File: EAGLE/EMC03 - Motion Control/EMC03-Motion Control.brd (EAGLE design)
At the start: 100 x 86.6 mm, 132 parts, among them J1 UART0, J10 S4B-PH-SM4, J11 S4B-PH-SM4, J12 S4B-PH-SM4, J13 S5B-PH-SM4, J14 S5B-PH-SM4, J15 S5B-PH-SM4, J17 S8B-PH-SM4, J19 S6B-PH-SM4, J2 FTSH-105-1-L-DV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

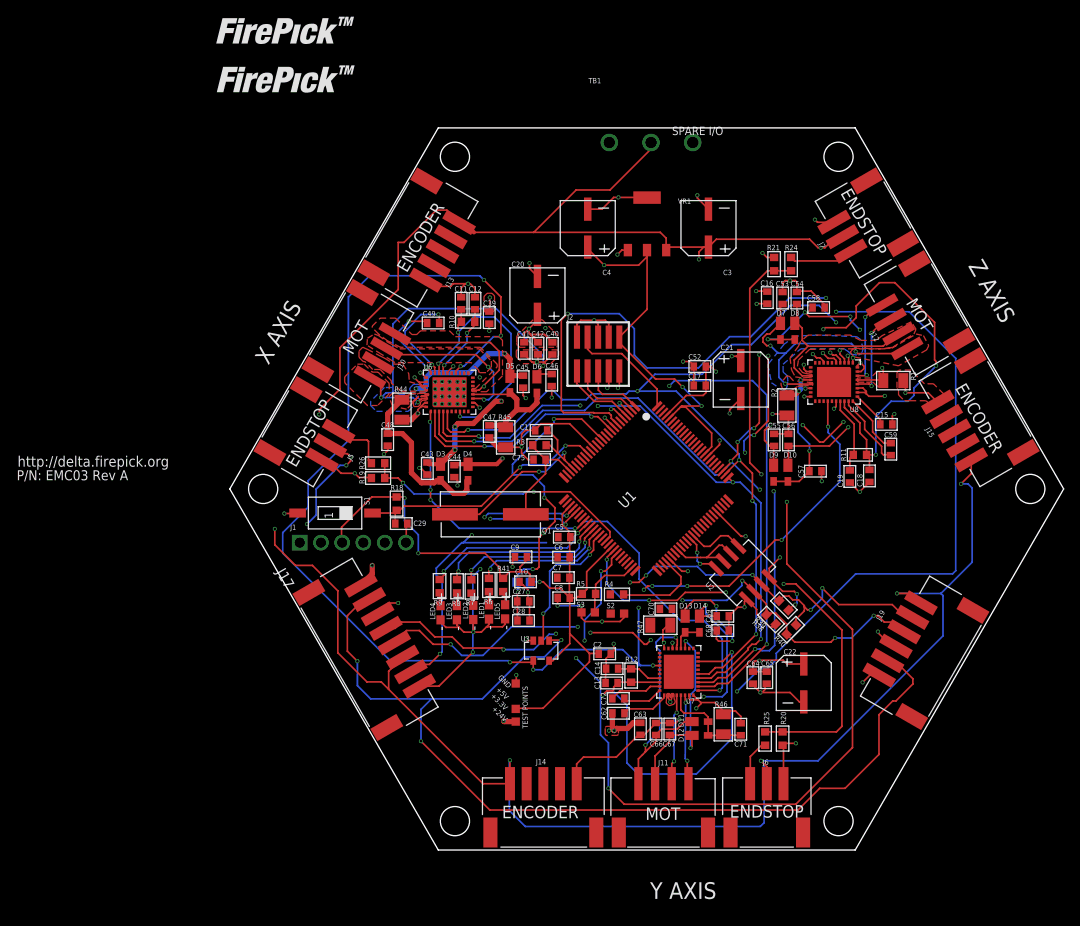
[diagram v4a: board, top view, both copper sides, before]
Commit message: Completed boards. Please look at airwires connecting thermal pads to GND vias. They shouldn't be present due to the vias.
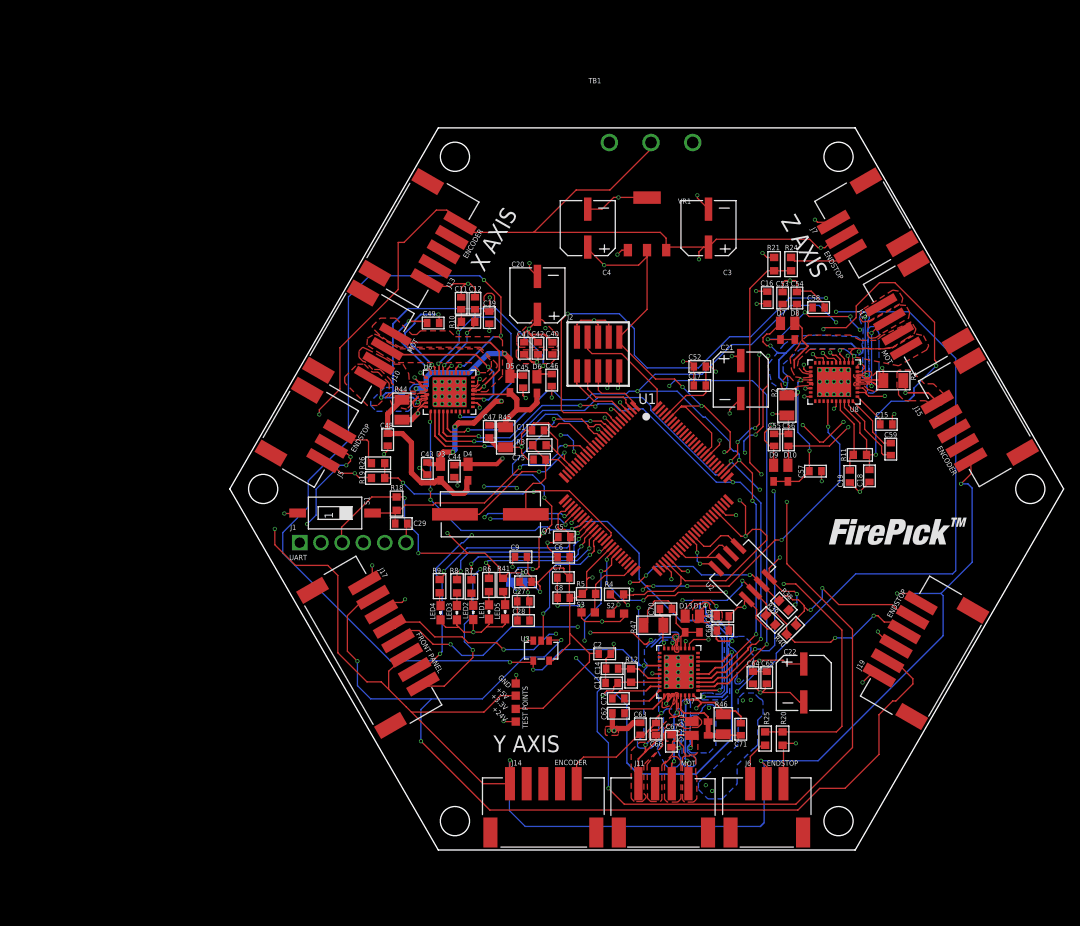
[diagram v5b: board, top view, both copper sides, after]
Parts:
- removed LOGO10: LOGO-FIREPICKLARGE, FirePick:LOGO-FIREPICK
- added TP2: +3.3V, TinWhiskers:TESTPAD
- moved LOGO12 94.9 mm to (71.6, 41.6)
- moved LOGO1 27.4 mm to (86.4, 41.4)
- moved C67 1.47 mm to (53.0, 19.7), turned to 270 degrees
- moved R47 0.83 mm to (50.8, 33.7)
- moved FB2 0.76 mm to (34.4, 38.8)
- moved J17 0.51 mm to (19.7, 32.7)
- moved C1 0.38 mm to (37.0, 57.0)
- moved J13 0.14 mm to (25.6, 78.4)
- moved J5 0.14 mm to (12.2, 55.1)
- moved J12 0.12 mm to (79.6, 69.5)
- moved J10 0.09 mm to (18.4, 65.9)
- moved R39 0.09 mm to (64.8, 34.3)
- moved J15 0.08 mm to (86.8, 57.0)
- moved J7 0.06 mm to (73.4, 80.2)
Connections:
- net +5V: now also TP2.PAD
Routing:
- net +3V3: track 166.0 -> 244.0 mm, vias 10 -> 20
- net 2A_2: track 25.3 -> 5.25 mm, vias 2 -> 3
- net 2B_2: track 29.8 -> 14.3 mm
- net GND: track 236.2 -> 251.5 mm, vias 58 -> 111
- net +5V: track 291.7 -> 306.6 mm
- net ISP_COM: track 0.00 -> 14.0 mm, vias 0 -> 3
- net 2A_3: track 23.4 -> 9.73 mm
- net USBMCU+: track 45.0 -> 34.6 mm
- net BRB2: track 3.87 -> 13.7 mm
- net 2B_3: track 32.5 -> 23.3 mm
- net DPWR: track 39.5 -> 44.3 mm
- net +24V: track 51.6 -> 53.1 mm, vias 17 -> 18
- net CLK: track 149.5 -> 150.4 mm
- net STAT_LED4: track 16.5 -> 17.4 mm
- net USBMCU-: track 36.4 -> 37.2 mm
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- added copper zone on layer 1, net 1A_2
- added copper zone on layer 15, net 1A_2
- added copper zone on layer 16, net 1A_2
- added copper zone on layer 1, net 1A_3
- added copper zone on layer 16, net 1A_3
- added copper zone on layer 1, net 1B_2
- added copper zone on layer 15, net 1B_2
- added copper zone on layer 16, net 1B_2
- added copper zone on layer 1, net 1B_3
- added copper zone on layer 16, net 1B_3
- added copper zone on layer 1, net 2A_2
- added copper zone on layer 15, net 2A_2
- added copper zone on layer 16, net 2A_2
- added copper zone on layer 1, net 2B_2
- added copper zone on layer 16, net 2B_2
- added copper zone on layer 1, net N$7
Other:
- board text added: "FRONT PANEL"
- board text added: "UART"
- board text removed: "P/N: EMC03 Rev A"
- board text removed: "SPARE I/O"
- board text removed: "http://delta.firepick.org"

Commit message: Updated all boards to include changes for production
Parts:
- S1: value SWS001 -> CPL-SW-MOM-147873-2; device smd-special:SMS-001 -> TinWhiskers:147873-2
- S2, S3: device TinWhiskers:0603 -> TinWhiskers:147873-2
- moved C14 3.95 mm to (42.2, 26.9)
- moved C13 3.93 mm to (42.2, 25.2)
- moved R12 3.72 mm to (44.5, 27.1)
- moved S2 3.28 mm to (46.8, 31.8), turned to 90 degrees
- moved S3 2.45 mm to (40.6, 34.5)
- moved C2 1.40 mm to (43.6, 30.2)
- moved S1 0.73 mm to (13.1, 47.7), turned to 0 degrees
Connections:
- net +3V3: now also VR1.P$1; no longer VR1.2
- net GND: no longer VR1.P$1
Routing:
- net +3V3: track 244.0 -> 258.8 mm, vias 20 -> 23
- net 1B_2: track 31.5 -> 21.8 mm, vias 4 -> 6
- net 1A_2: track 24.2 -> 18.3 mm, vias 9 -> 11
- net N$5: track 5.45 -> 9.32 mm
- net 2B_2: track 14.3 -> 11.2 mm, vias 2 -> 3
- net N$6: track 48.0 -> 51.0 mm
- net RESET: track 31.8 -> 33.6 mm
- net 2A_2: track 5.25 -> 3.65 mm, vias 3 -> 6
- net DFU: track 8.60 -> 9.75 mm
- net B: track 76.5 -> 77.5 mm, vias 7 -> 8
- net ISP_COM: track 14.0 -> 15.0 mm
- net !ENABLE_LPC: track 17.3 -> 18.0 mm
- net GND: track 251.5 -> 251.2 mm, vias 111 -> 110

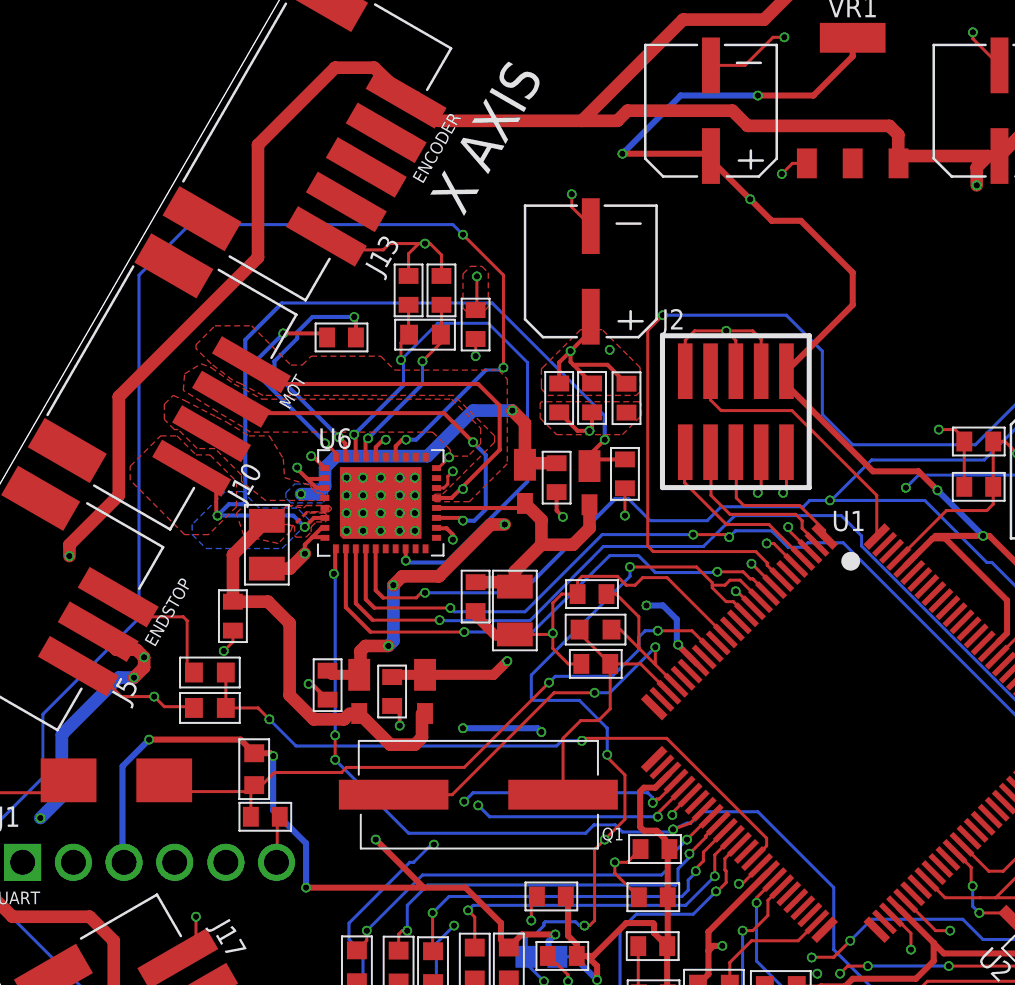
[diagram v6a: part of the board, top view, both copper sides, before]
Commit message: Updated motor hole size to 7mm Dia. Rerouted around.
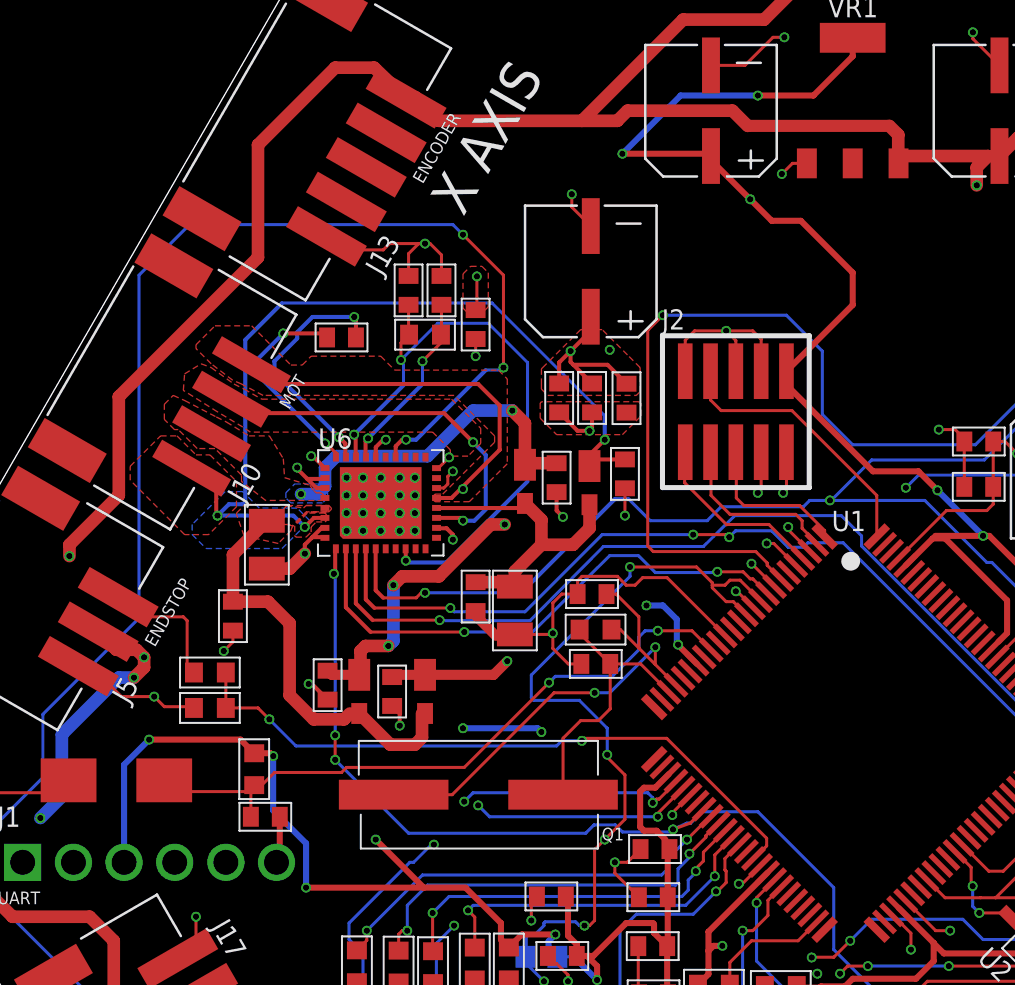
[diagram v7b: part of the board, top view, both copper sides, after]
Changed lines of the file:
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@@
 <layer number="23" name="tOrigins" color="15" fill="1" visible="yes" active="yes"/>
 <layer number="24" name="bOrigins" color="15" fill="1" visible="yes" active="yes"/>
-<layer number="25" name="tNames" color="7" fill="1" visible="yes" active="yes"/>
-<layer number="26" name="bNames" color="7" fill="1" visible="yes" active="yes"/>
+<layer number="25" name="tNames" color="7" fill="1" visible="no" active="yes"/>
+<layer number="26" name="bNames" color="7" fill="1" visible="no" active="yes"/>
 <layer number="27" name="tValues" color="7" fill="1" visible="no" active="yes"/>
 <layer number="28" name="bValues" color="7" fill="1" visible="no" active="yes"/>
-<layer number="29" name="tStop" color="7" fill="3" visible="yes" active="yes"/>
-<layer number="30" name="bStop" color="7" fill="6" visible="yes" active="yes"/>
-<layer number="31" name="tCream" color="7" fill="4" visible="yes" active="yes"/>
-<layer number="32" name="bCream" color="7" fill="5" visible="yes" active="yes"/>
+<layer number="29" name="tStop" color="7" fill="3" visible="no" active="yes"/>
+<layer number="30" name="bStop" color="7" fill="6" visible="no" active="yes"/>
+<layer number="31" name="tCream" color="7" fill="4" visible="no" active="yes"/>
+<layer number="32" name="bCream" color="7" fill="5" visible="no" active="yes"/>
 <layer number="33" name="tFinish" color="6" fill="3" visible="no" active="yes"/>
 <layer number="34" name="bFinish" color="6" fill="6" visible="no" active="yes"/>
@@
 <wire x1="41.529" y1="27.7495" x2="41.529" y2="26.887" width="0.2032" layer="1"/>
 <wire x1="41.529" y1="26.887" x2="41.5025" y2="26.8605" width="0.2032" layer="1"/>
-<wire x1="72.4535" y1="62.865" x2="72.463" y2="62.827" width="0" layer="19" extent="1-1"/>
-<wire x1="53.848" y1="28.067" x2="53.7845" y2="28.0035" width="0" layer="19" extent="1-1"/>
-<wire x1="26.3525" y1="61.595" x2="26.3525" y2="61.976" width="0" layer="19" extent="1-1"/>
 <wire x1="42.037" y1="28.2575" x2="43.053" y2="28.2575" width="0.2032" layer="1"/>
 <wire x1="43.053" y1="28.2575" x2="43.688" y2="28.8925" width="0.2032" layer="1"/>
@@
 <wire x1="6.5405" y1="47.0535" x2="10.065334375" y2="47.0535" width="0.1524" layer="1"/>
 <wire x1="10.065334375" y1="47.0535" x2="10.687128125" y2="47.67529375" width="0.1524" layer="1"/>
+<wire x1="72.4535" y1="62.865" x2="72.463" y2="62.827" width="0" layer="19" extent="1-1"/>
+<wire x1="53.848" y1="28.067" x2="53.7845" y2="28.0035" width="0" layer="19" extent="1-1"/>
+<wire x1="26.3525" y1="61.595" x2="26.3525" y2="61.976" width="0" layer="19" extent="1-1"/>
 </signal>
 <signal name="X_STOP">
@@
 <wire x1="28.0814" y1="81.9641" x2="29.2735" y2="80.772" width="0.635" layer="1"/>
 <wire x1="29.2735" y1="80.772" x2="36.449" y2="80.772" width="0.635" layer="1"/>
-<wire x1="51.6255" y1="80.772" x2="51.8795" y2="80.518" width="0" layer="19" extent="1-16"/>
 <wire x1="51.8795" y1="80.518" x2="52.324" y2="80.0735" width="0.635" layer="1"/>
 <wire x1="52.324" y1="80.0735" x2="52.324" y2="78.652" width="0.635" layer="1"/>
@@
 <wire x1="38.735" y1="81.28" x2="44.0055" y2="81.28" width="0.635" layer="1"/>
 <wire x1="44.0055" y1="81.28" x2="44.7675" y2="80.518" width="0.635" layer="1"/>
-<wire x1="44.7675" y1="80.518" x2="51.8795" y2="80.518" width="0.635" layer="1"/>
+<wire x1="44.7675" y1="80.518" x2="51.8795" y2="80.518" width="0.6096" layer="1"/>
 </signal>
 <signal name="Y_STOP">
@@
 <contactref element="J1" pad="6"/>
 <contactref element="C29" pad="1"/>
-<wire x1="21.1593" y1="43.5237" x2="21.1593" y2="45.72" width="0.1524" layer="1"/>
-<wire x1="21.1593" y1="45.72" x2="21.2863" y2="45.847" width="0.1524" layer="1"/>
-<wire x1="21.1593" y1="43.5237" x2="21.122" y2="43.561" width="0" layer="19" extent="1-1"/>
+<wire x1="21.2863" y1="45.847" x2="21.2863" y2="43.7253" width="0.3048" layer="1"/>
+<wire x1="21.2863" y1="43.7253" x2="21.122" y2="43.561" width="0.3048" layer="1"/>
 </signal>
 <signal name="+3V3">
@@
 <wire x1="39.751" y1="28.8925" x2="38.8025" y2="28.8925" width="0.3048" layer="1"/>
 <wire x1="38.8025" y1="28.8925" x2="38.288" y2="29.407" width="0.3048" layer="1"/>
-<wire x1="13.3985" y1="43.6345" x2="13.3985" y2="48.387" width="0.3048" layer="16"/>
-<wire x1="13.3985" y1="48.387" x2="14.732" y2="49.7205" width="0.3048" layer="16"/>
 <via x="14.732" y="49.7205" extent="1-16" drill="0.3048"/>
 <wire x1="14.732" y1="49.7205" x2="19.317503125" y2="49.7205" width="0.3048" layer="1"/>
 <wire x1="19.317503125" y1="49.7205" x2="20.0025" y2="49.035503125" width="0.3048" layer="1"/>
-<wire x1="13.3985" y1="43.6345" x2="13.472" y2="43.561" width="0" layer="19" extent="16-16"/>
+<wire x1="13.472" y1="43.561" x2="13.472" y2="48.4605" width="0.3048" layer="16"/>
+<wire x1="13.472" y1="48.4605" x2="14.732" y2="49.7205" width="0.3048" layer="16"/>
 </signal>
 <signal name="RESET">

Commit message: Final(??) Versions of FPD boards.
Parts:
- removed LOGO1, LOGO12: LOGO-FIREPICKLARGE, FirePick:LOGO-FIREPICK
- added U$1, U$2: TIN-WHISKERSSMALL, !tin-whiskers-logo:TIN-WHISKERS-SMALL
